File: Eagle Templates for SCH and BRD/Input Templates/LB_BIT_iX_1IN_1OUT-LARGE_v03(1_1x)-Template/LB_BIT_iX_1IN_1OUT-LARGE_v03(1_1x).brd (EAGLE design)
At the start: 21.4 x 24.8 mm, 17 parts, among them U1 LV321SOT23-5, U2 LV321SOT23-5

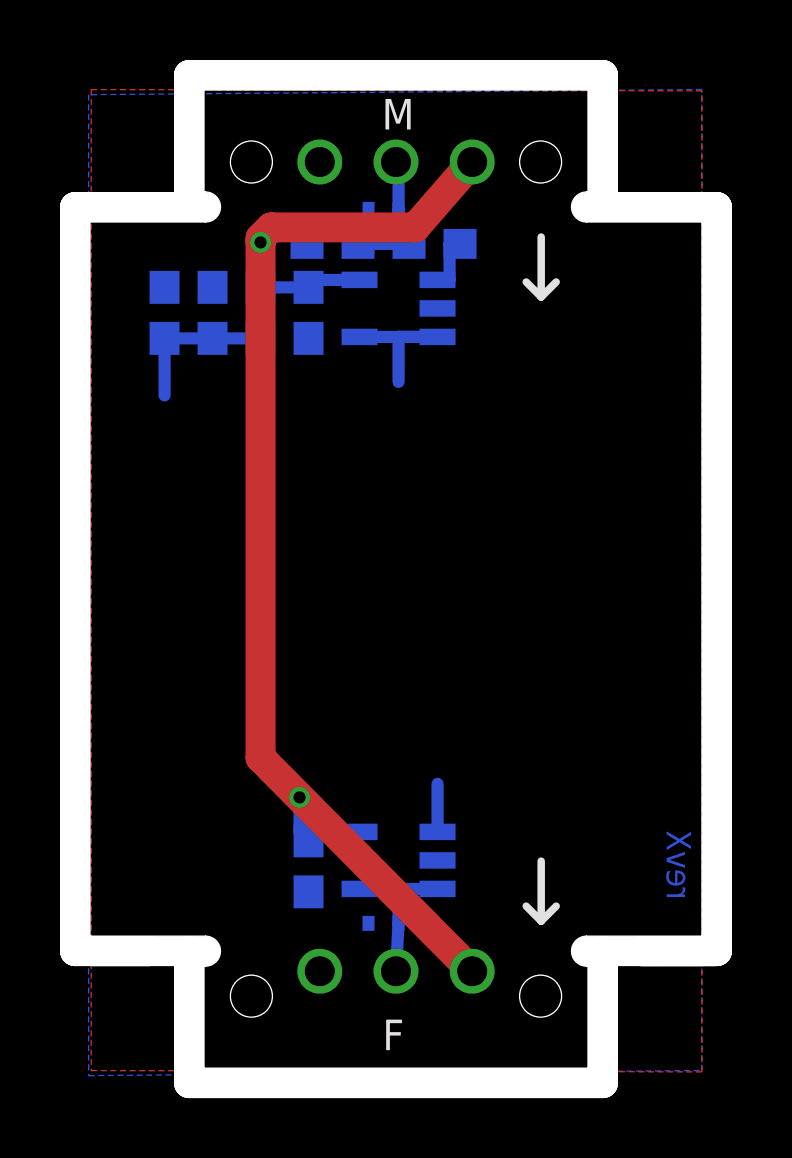
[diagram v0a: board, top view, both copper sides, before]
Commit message: added bitlab logo and made minor changes to board templates. Updated littlebits library.
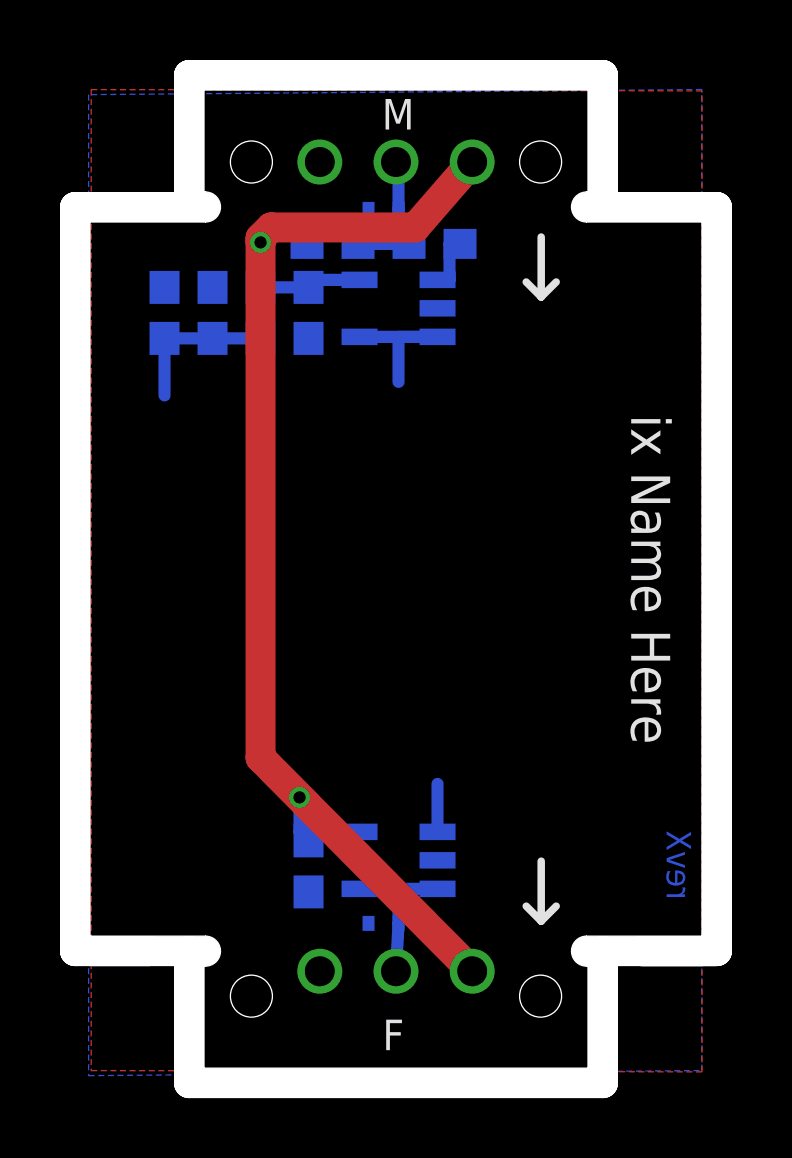
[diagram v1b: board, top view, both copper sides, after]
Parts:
- added U$3: (no value), LITTLEBITS:BITLAB-LOGO
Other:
- board text added: "ix Name Here"
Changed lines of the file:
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@@
 <layer number="113" name="extra" color="10" fill="1" visible="yes" active="yes"/>
 <layer number="116" name="Patch_BOT" color="9" fill="4" visible="yes" active="yes"/>
+<layer number="118" name="Rect_Pads" color="7" fill="1" visible="no" active="yes"/>
 <layer number="121" name="_tsilk" color="7" fill="1" visible="yes" active="yes"/>
 <layer number="122" name="_bsilk" color="7" fill="1" visible="yes" active="yes"/>
@@
 <wire x1="2.51" y1="26.745" x2="2.51" y2="28.915" width="1" layer="46"/>
 <wire x1="2.51" y1="28.915" x2="5" y2="28.915" width="1" layer="46"/>
+<text x="21.7" y="16.5" size="1.3" layer="21" font="vector" rot="SR270" align="center">ix Name Here</text>
 </plain>
 <attributes>
@@
 <element name="FRAME1" library="LITTLEBITS" package="FABDWG01-OHW" value="FRAME-LETTER" x="0" y="0"/>
 <element name="U$2" library="ohw-logo" package="OSHW_FILLX150_NOTEXT" value="" x="18.9" y="23" rot="MR90"/>
+<element name="U$3" library="LITTLEBITS" package="BITLAB-LOGO" value="" x="19.8" y="21" rot="R270"/>
 </elements>
 <signals>

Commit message: Updated templates
- Added ferrite beads
- Moved text and annotations off of Nets layer
- Minor layout changes
- Removed I/O/W prefix from reference designators
- Removed output stage components from output bits
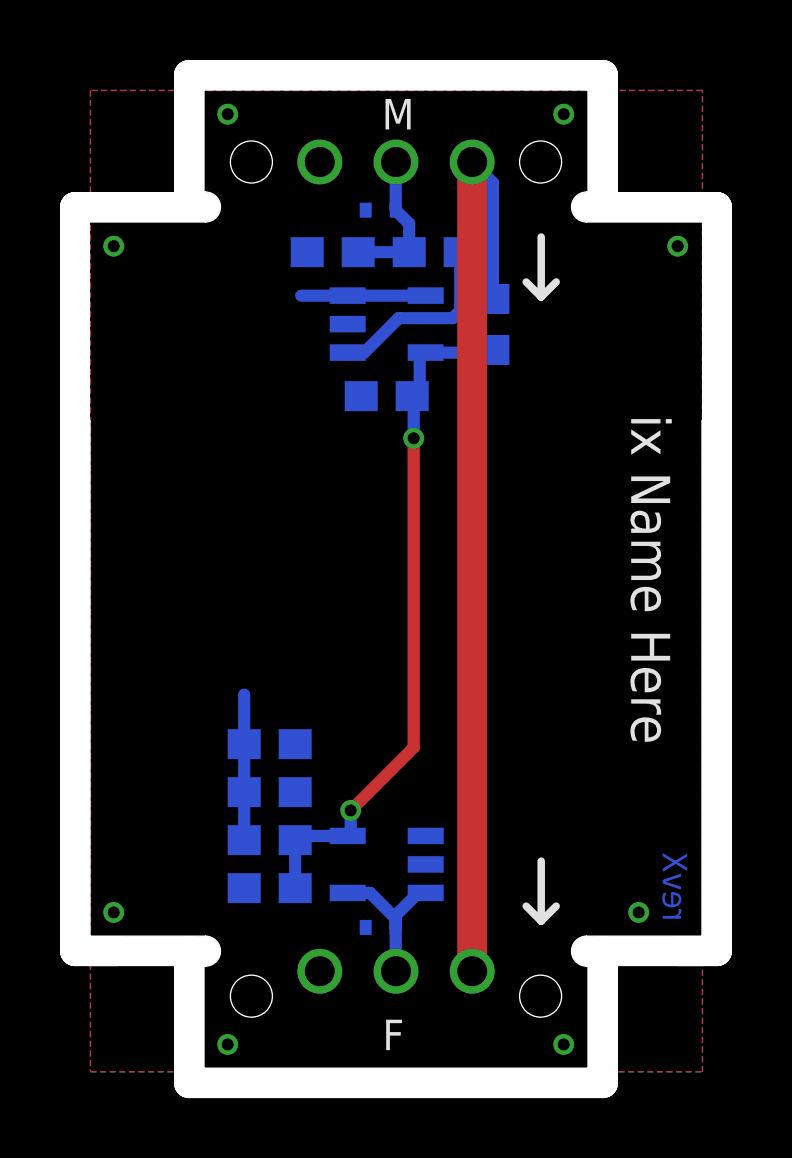
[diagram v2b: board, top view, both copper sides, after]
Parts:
- removed FRAME1: FRAME-LETTER, LITTLEBITS:FABDWG01-OHW
- removed I?C1: 0.1uF, LITTLEBITS:CAP-0603
- removed I?C2: 10uF, LITTLEBITS:CAP-0603
- removed I?C3: 1.0uF, LITTLEBITS:CAP-0603
- removed I?R1: 1meg, LITTLEBITS:RES-0603
- removed I?R2: 10K, LITTLEBITS:RES-0603
- removed I?R3, I?R4: 3K3, LITTLEBITS:RES-0603
- removed I?TVS1, I?TVS2: ESD9B5.0ST5G, LITTLEBITS:SOD-923
- added C1: 0.1uF, LITTLEBITS:CAP-0603
- added C2: 10uF, LITTLEBITS:CAP-0603
- added C3: 1.0uF, LITTLEBITS:CAP-0603
- added FB1: FERRITE-BEAD0603, LITTLEBITS:R0603
- added R1: 1meg, LITTLEBITS:RES-0603
- added R2: 10K, LITTLEBITS:RES-0603
- added R3, R4: 3K3, LITTLEBITS:RES-0603
- added TVS1, TVS2: ESD9B5.0ST5G, LITTLEBITS:SOD-923
- added U$5: (no value), LITTLEBITS:BITLAB-LOGO
- U$1: value OSHWCREDIT -> OSHW-LOGOL; device LITTLEBITS:OSHWCREDIT -> LITTLEBITS131206:OSHW-LOGO-L
- U$2: value (none) -> OSHWCREDIT; device ohw-logo:OSHW_FILLX150_NOTEXT -> LITTLEBITS:OSHWCREDIT
- U$3: value (none) -> FRAME-LETTER; device LITTLEBITS:BITLAB-LOGO -> LITTLEBITS:FABDWG01-OHW
- U$4: value OSHW-LOGOL -> (none); device LITTLEBITS131206:OSHW-LOGO-L -> ohw-logo:OSHW_FILLX150_NOTEXT
- moved U$2 141.3 mm to (-92.2, -64.3), flipped to the top, turned to 0 degrees
- moved U$4 106.6 mm to (18.9, 23.0), flipped to the bottom, turned to 90 degrees
- moved U$1 58.3 mm to (-37.5, -68.2)
- moved U$3 28.9 mm to (0.00, 0.00), turned to 0 degrees
- moved U1 0.66 mm to (12.9, 25.0), turned to 90 degrees
- moved U2 0.42 mm to (12.9, 7.00)
- renumbered I?BSF to BSF1, I?BSM to BSM1
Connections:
- new net LB_VCC: BSF1.VCC, BSM1.VCC1, FB1.2
- net GND: now also C1.2, C2.2, C3.1, R1.1, R4.1, TVS1.1, TVS2.1; no longer I?C1.2, I?C2.2, I?C3.1, I?R1.1, I?R4.1, I?TVS1.1, I?TVS2.1
- net N$4: now also R2.1; no longer I?R2.1
- net SIG_IN: now also R1.2, R2.2, TVS1.2; no longer I?R1.2, I?R2.2, I?TVS1.2
- net SIG_OUT: now also TVS2.2; no longer I?TVS2.2
- net VCC: now also C1.1, C3.2, FB1.1, R3.2; no longer BSF1.VCC, BSM1.VCC1, I?C1.1, I?C3.2, I?R3.2
- net VREF: now also C2.1, R3.1, R4.2; no longer I?C2.1, I?R3.1, I?R4.2
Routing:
- net LB_VCC: track 0.00 -> 31.8 mm
- net VCC: track 46.1 -> 23.6 mm
- net N$4: track 1.95 -> 6.28 mm
- net N$3: track 1.60 -> 0.00 mm
- net N$2: track 5.40 -> 4.15 mm
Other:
- outline, holes or cut-outs redrawn
